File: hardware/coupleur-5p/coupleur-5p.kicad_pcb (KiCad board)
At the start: 4 copper layers, 110 x 30 mm, 12 parts, among them J1 RJ45, J2 Conn_01x04, J3 RJ45, J4 RJ45, J5 RJ45, J6 RJ45

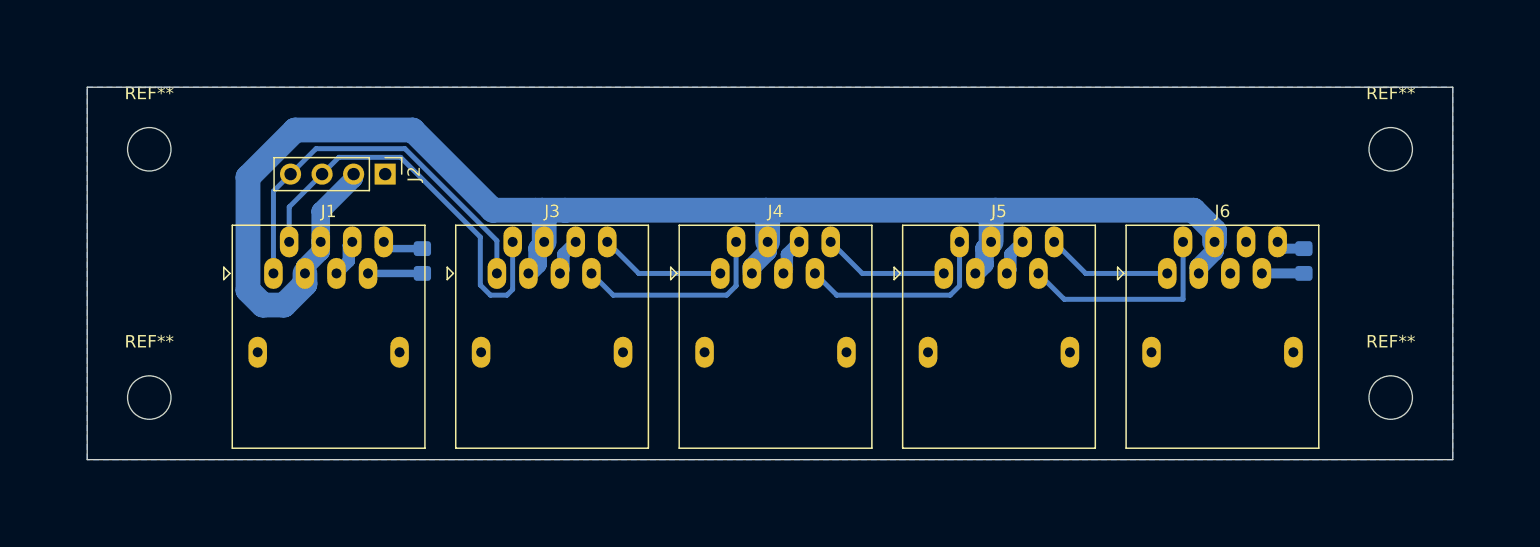
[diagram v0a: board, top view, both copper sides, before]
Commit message: Add 5mm margin around PCBs
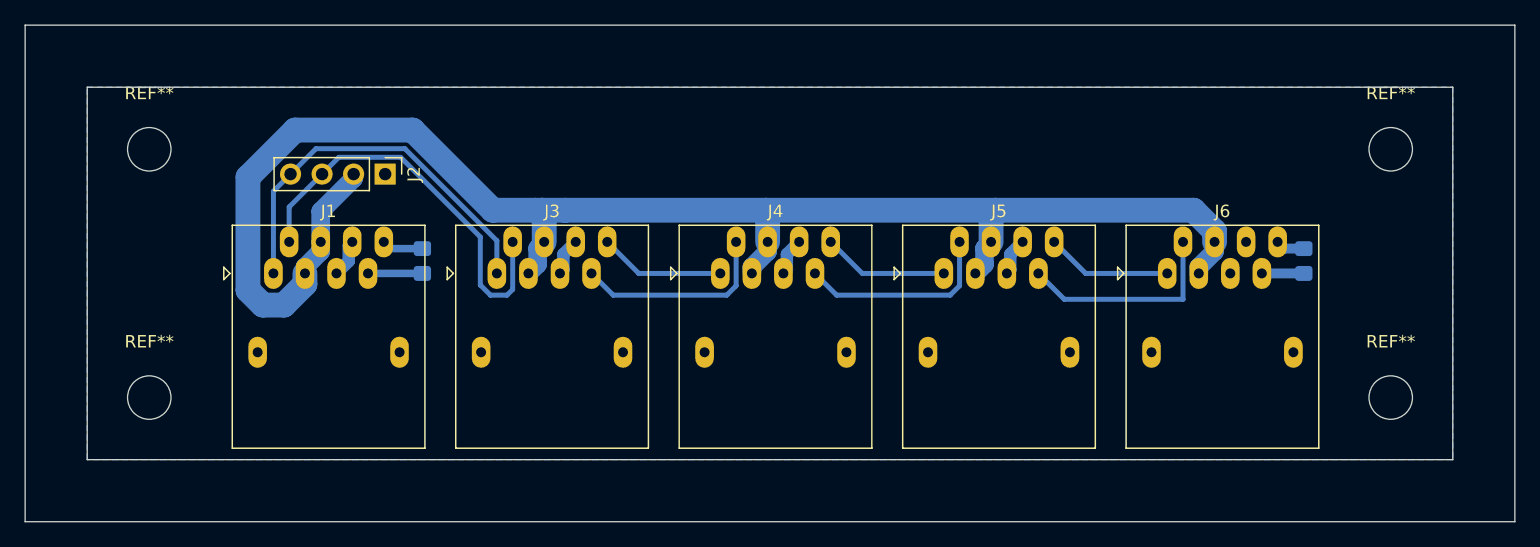
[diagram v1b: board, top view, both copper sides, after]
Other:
- board size 110 x 30 mm -> 120 x 40 mm

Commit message: Only 2 layers
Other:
- copper layers 4 -> 2
